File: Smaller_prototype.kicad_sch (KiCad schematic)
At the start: 8 parts, among them SW3 SW_Push, SW4 SW_Push, SW5 SW_Push, SW6 SW_Push

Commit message: -add some changes to power section and display
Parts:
- added C16, C17, C18, C19, C20: 1u, Capacitor_SMD:C_0603_1608Metric_Pad1.08x0.95mm_HandSolder, symbol Device:C
- added R27: DNP, Resistor_SMD:R_0603_1608Metric_Pad0.98x0.95mm_HandSolder, symbol Device:R
- added R37, R38: R, Resistor_SMD:R_0603_1608Metric_Pad0.98x0.95mm_HandSolder, symbol Device:R
- added SW7: SW_Push, Button_Switch_SMD:SW_SPST_B3S-1000, symbol Switch:SW_Push
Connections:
- net +3.3V: now also R27.1
- net GND: now also C16.2, C17.2, C18.2, C19.2, C20.2, R38.1, SW7.1
- net MCU/GPIO_14/JTAG_TMS: now also R37.1, R38.2
- net SW1: now also C20.1
- net SW2: now also C19.1
- net SW3: now also C18.1
- net SW4: now also C17.1
- new net Charger_plugged_in?: R37.2
- new net SW5: C16.1, R27.2, SW7.2
- no-connect marks 8 -> 6
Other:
- sheet Display ports: added Display_TP_RST, TP_SCL, TP_SDA; removed Display_TP_CS
- sheet MCU ports: added GPIO_43/TXD0, GPIO_44/RXD0, I2C_SCL, I2C_SDA; removed GPIO_1/TXD0, GPIO_3/RXD0
- moved on the sheet: R10, R11, R12, R9, SW3, SW4, SW5, SW6

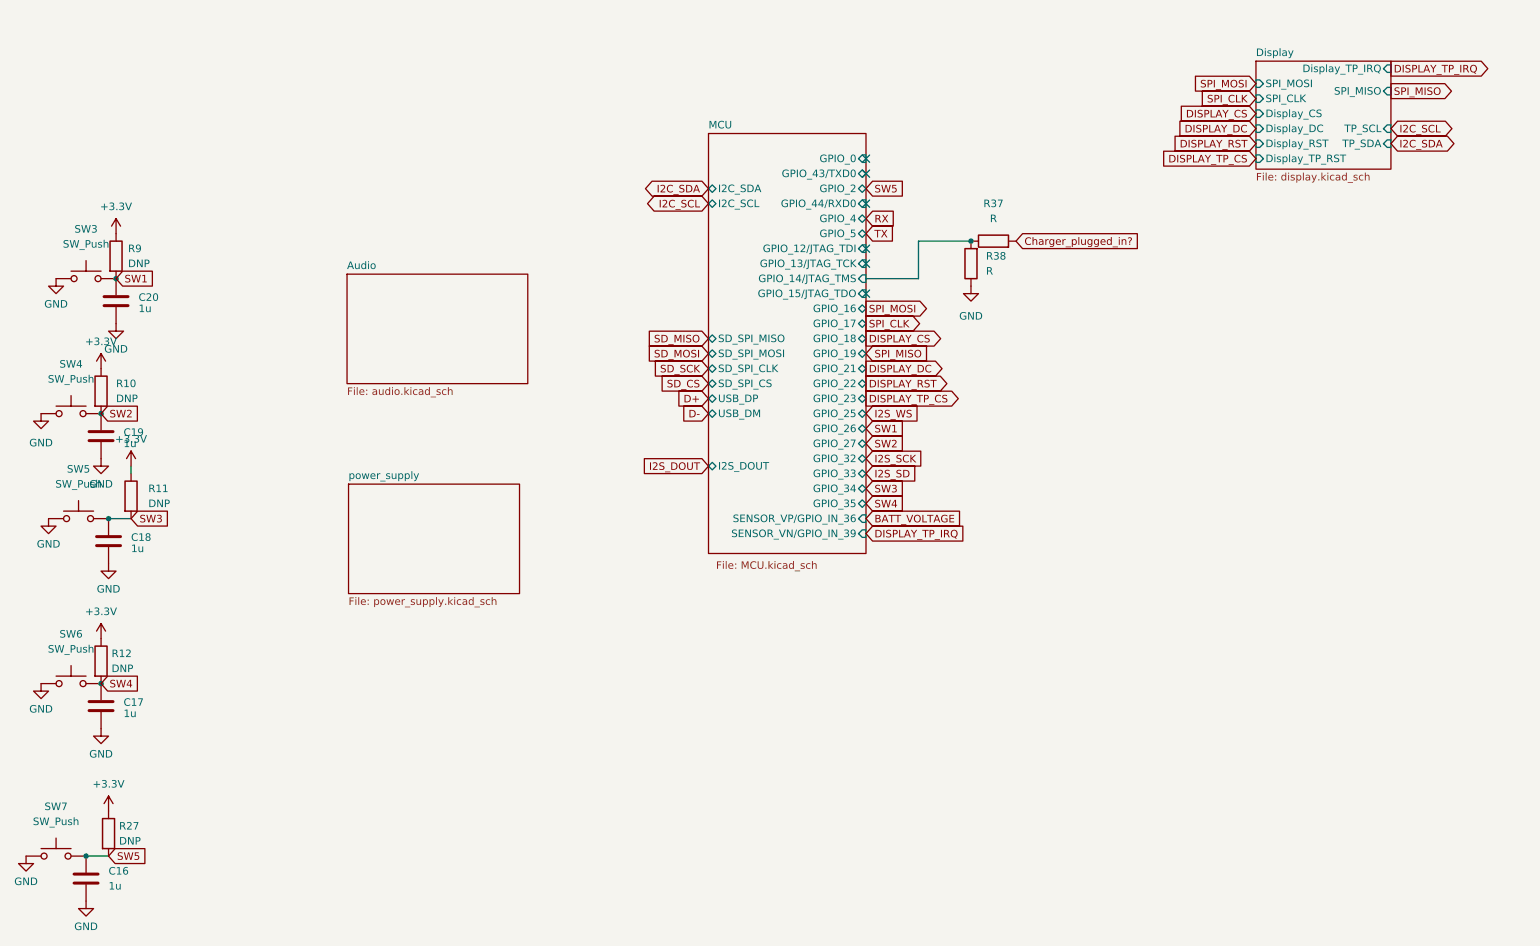
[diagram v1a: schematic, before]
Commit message: -enh repin mcu in schematic
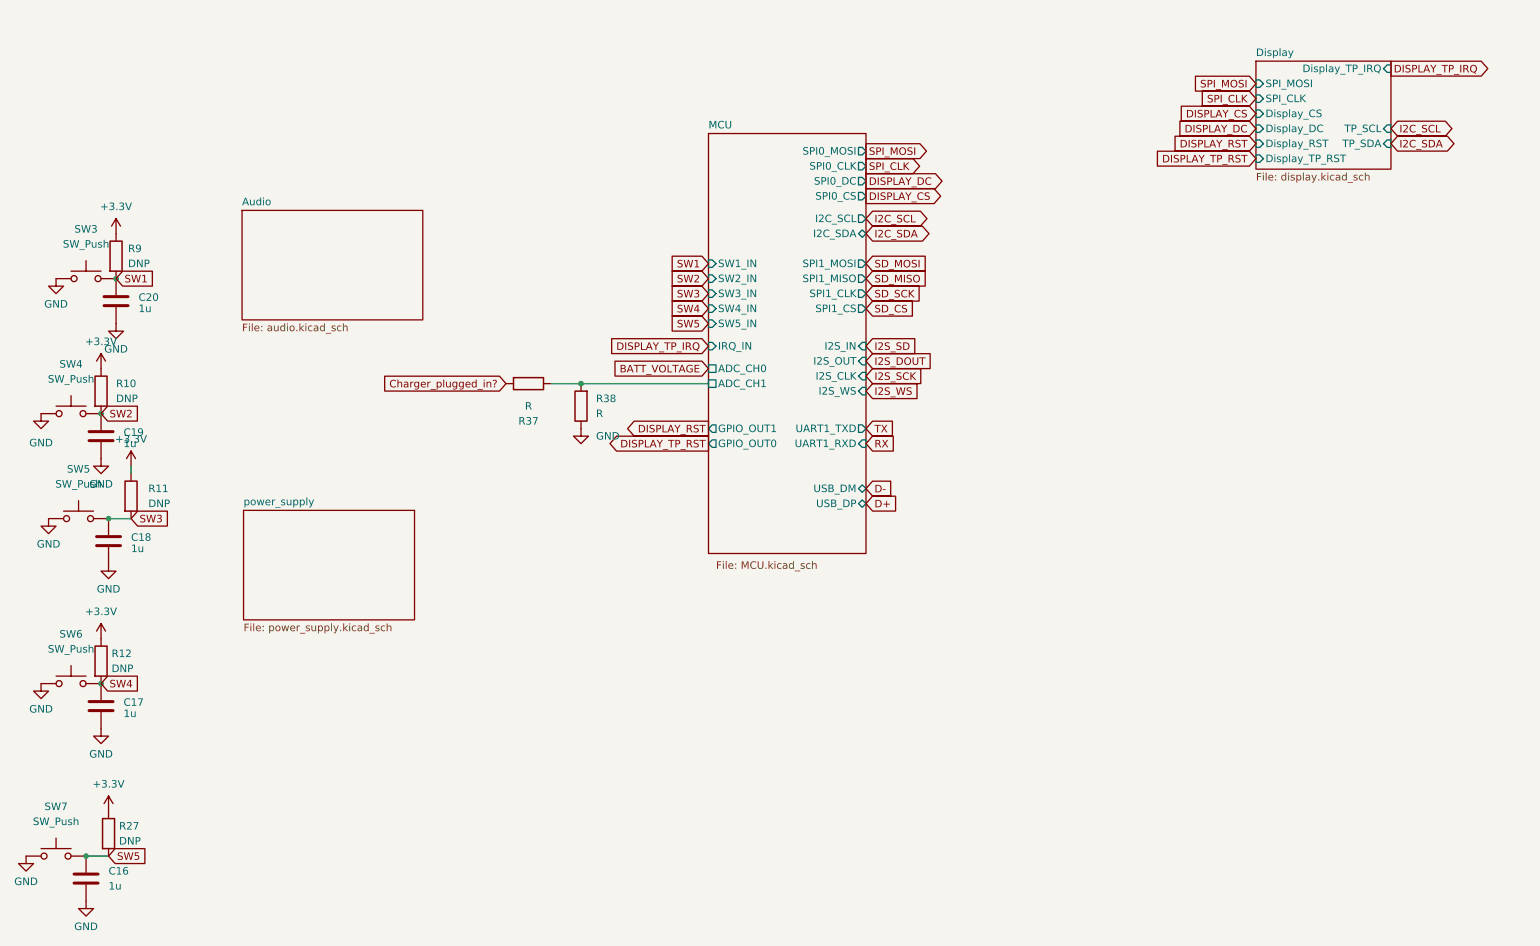
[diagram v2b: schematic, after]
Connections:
- net MCU/GPIO_14/JTAG_TMS renamed MCU/ADC_CH1
- no-connect marks 6 -> 0
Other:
- sheet Display ports: added none; removed SPI_MISO
- sheet MCU ports: added ADC_CH0, ADC_CH1, GPIO_OUT0, GPIO_OUT1, I2S_CLK, I2S_IN, I2S_OUT, I2S_WS, IRQ_IN, SPI0_CLK, SPI0_CS, SPI0_DC, SPI0_MOSI, SPI1_CLK, SPI1_CS, SPI1_MISO, SPI1_MOSI, SW1_IN, SW2_IN, SW3_IN, SW4_IN, SW5_IN, UART1_RXD, UART1_TXD; removed GPIO_0, GPIO_12/JTAG_TDI, GPIO_13/JTAG_TCK, GPIO_14/JTAG_TMS, GPIO_15/JTAG_TDO, GPIO_16, GPIO_17, GPIO_18, GPIO_19, GPIO_2, GPIO_21, GPIO_22, GPIO_23, GPIO_25, GPIO_26, GPIO_27, GPIO_32, GPIO_33, GPIO_34, GPIO_35, GPIO_4, GPIO_43/TXD0, GPIO_44/RXD0, GPIO_5, I2S_DOUT, SD_SPI_CLK, SD_SPI_CS, SD_SPI_MISO, SD_SPI_MOSI, SENSOR_VN/GPIO_IN_39, SENSOR_VP/GPIO_IN_36
- moved on the sheet: R37, R38

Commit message: -add soft latching circuit, routing mostly done
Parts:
- added R35, R36: DNP, Resistor_SMD:R_0603_1608Metric_Pad0.98x0.95mm_HandSolder, symbol Device:R
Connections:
- net SW3: now also R35.2; no longer C18.1, R11.2, SW5.2
- new net: C18.1, R11.2, R35.1, R36.2, SW5.2
- new net Power_latching_circuit: R36.1
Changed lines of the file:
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@@
+	)
+	(junction
+		(at 36.83 105.41)
+		(diameter 0)
+		(color 0 0 0 0)
 	)
 	(junction
@@
 	(global_label "SW3"
 		(shape input)
-		(at 36.83 105.41 0)
-		(fields_autoplaced yes)
-		(effects
-			(font
-				(size 1.27 1.27)
-			)
-			(justify left)
-		)
-		(property "Intersheetrefs" "${INTERSHEET_REFS}"
-			(at 43.6856 105.41 0)
+		(at 44.45 105.41 0)
+		(fields_autoplaced yes)
+		(effects
+			(font
+				(size 1.27 1.27)
+			)
+			(justify left)
+		)
+		(property "Intersheetrefs" "${INTERSHEET_REFS}"
+			(at 51.3056 105.41 0)
 			(effects
 				(font
@@
 		(property "Intersheetrefs" "${INTERSHEET_REFS}"
 			(at 175.3424 48.26 0)
+			(effects
+				(font
+					(size 1.27 1.27)
+				)
+				(justify left)
+				(hide yes)
+			)
+		)
+	)
+	(global_label "Power_latching_circuit"
+		(shape input)
+		(at 36.83 113.03 0)
+		(fields_autoplaced yes)
+		(effects
+			(font
+				(size 1.27 1.27)
+			)
+			(justify left)
+		)
+		(property "Intersheetrefs" "${INTERSHEET_REFS}"
+			(at 61.1027 113.03 0)
 			(effects
 				(font
@@
 	)
 	(symbol
+		(lib_id "Device:R")
+		(at 36.83 109.22 180)
+		(unit 1)
+		(exclude_from_sim no)
+		(in_bom yes)
+		(on_board yes)
+		(dnp no)
+		(fields_autoplaced yes)
+		(property "Reference" "R36"
+			(at 39.37 107.9499 0)
+			(effects
+				(font
+					(size 1.27 1.27)
+				)
+				(justify right)
+			)
+		)
+		(property "Value" "DNP"
+			(at 39.37 110.4899 0)
+			(effects
+				(font
+					(size 1.27 1.27)
+				)
+				(justify right)
+			)
+		)
+		(property "Footprint" "Resistor_SMD:R_0603_1608Metric_Pad0.98x0.95mm_HandSolder"
+			(at 38.608 109.22 90)
+			(effects
+				(font
+					(size 1.27 1.27)
+				)
+				(hide yes)
+			)
+		)
+		(property "Datasheet" "~"
+			(at 36.83 109.22 0)
+			(effects
+				(font
+					(size 1.27 1.27)
+				)
+				(hide yes)
+			)
+		)
+		(property "Description" ""
+			(at 36.83 109.22 0)
+			(effects
+				(font
+					(size 1.27 1.27)
+				)
+				(hide yes)
+			)
+		)
+		(pin "1"
+		)
+		(pin "2"
+		)
+		(instances
+			(project "Smaller_prototype"
+				(path "/9afce839-94a1-420a-b951-50ad17fc2524"
+					(reference "R36")
+					(unit 1)
+				)
+			)
+		)
+	)
+	(symbol
 		(lib_id "Device:C")
 		(at 29.21 166.37 0)
@@
 					(unit 1)
 				)
+			)
+		)
+	)
+	(symbol
+		(lib_id "Device:R")
+		(at 40.64 105.41 90)
+		(unit 1)
+		(exclude_from_sim no)
+		(in_bom yes)
+		(on_board yes)
+		(dnp no)
+		(fields_autoplaced yes)
+		(property "Reference" "R35"
+			(at 40.64 99.06 90)
+			(effects
+				(font
+					(size 1.27 1.27)
+				)
+			)
+		)
+		(property "Value" "DNP"
+			(at 40.64 101.6 90)
+			(effects
+				(font
+					(size 1.27 1.27)
+				)
+			)
+		)
+		(property "Footprint" "Resistor_SMD:R_0603_1608Metric_Pad0.98x0.95mm_HandSolder"
+			(at 40.64 107.188 90)
+			(effects
+				(font
+					(size 1.27 1.27)
+				)
+				(hide yes)
+			)
+		)
+		(property "Datasheet" "~"
+			(at 40.64 105.41 0)
+			(effects
+				(font
+					(size 1.27 1.27)
+				)
+				(hide yes)
+			)
+		)
+		(property "Description" ""
+			(at 40.64 105.41 0)
+			(effects
+				(font
+					(size 1.27 1.27)
+				)
+				(hide yes)
+			)
+		)
+		(pin "1"
+		)
+		(pin "2"
+		)
+		(instances
+			(project "Smaller_prototype"
+				(path "/9afce839-94a1-420a-b951-50ad17fc2524"
+					(reference "R35")
+					(unit 1)
+				)

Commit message: -add end revision
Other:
- sheet Display ports: added SPI_MISO; removed none
- sheet MCU ports: added SPI0_MISO; removed none
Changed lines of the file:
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@@
 		)
 	)
+	(global_label "SPI_MISO"
+		(shape input)
+		(at 134.62 44.45 180)
+		(fields_autoplaced yes)
+		(effects
+			(font
+				(size 1.27 1.27)
+			)
+			(justify right)
+		)
+		(property "Intersheetrefs" "${INTERSHEET_REFS}"
+			(at 122.9867 44.45 0)
+			(effects
+				(font
+					(size 1.27 1.27)
+				)
+				(justify right)
+				(hide yes)
+			)
+		)
+	)
 	(global_label "I2S_WS"
 		(shape input)
@@
 		)
 	)
+	(global_label "SPI_MISO"
+		(shape output)
+		(at 250.19 34.29 0)
+		(fields_autoplaced yes)
+		(effects
+			(font
+				(size 1.27 1.27)
+			)
+			(justify left)
+		)
+		(property "Intersheetrefs" "${INTERSHEET_REFS}"
+			(at 261.8233 34.29 0)
+			(effects
+				(font
+					(size 1.27 1.27)
+				)
+				(justify left)
+				(hide yes)
+			)
+		)
+	)
 	(global_label "I2S_DOUT"
 		(shape input)
@@
 			)
 		)
+		(pin "SPI_MISO" output
+			(at 250.19 34.29 0)
+			(effects
+				(font
+					(size 1.27 1.27)
+				)
+				(justify right)
+			)
+		)
 		(instances
 			(project "Testapparaat"
@@
 			(effects
 				(font
+					(size 1.27 1.27)
+				)
+				(justify left)
+			)
+		)
+		(pin "SPI0_MISO" input
+			(at 134.62 44.45 180)
+			(effects
+				(font
